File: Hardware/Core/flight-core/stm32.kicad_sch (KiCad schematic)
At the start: 33 parts, among them J1 Conn_01x04_Socket, SW1 SW_Push, SW2 SW_Push, U1 STM32G473CCTx, U13 MCP23S17_SS, U402 TCAN1042VDRQ1, U92 CC56-12SEKWA, U98 MAX7221xWG, Y1 48 MHZ

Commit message: updated all top sheets
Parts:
- removed TP_STM_IO2: TP, footprints:tp_1.6mm, symbol formula:TP
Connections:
- net CTRL_SANITY_CHECK is gone; now on net CORE_HEARTBEAT: U1.39 (PA15)
- net GPIO_SENSE3 is gone; now on net SHDN_SENSE_BMS_OK_ALL: U13.28 (GPA7)
- net CORE_HEARTBEAT: no longer U1.29 (PB15)
- net DEBUG1: now also U1.25 (PB11); no longer U1.28 (PB14)
- net DEBUG2: now also U13.22 (GPA1); no longer U13.27 (GPA6)
- net SHDN_SENSE_BMS_OK_ALL: no longer U13.26 (GPA5)
- net SHDN_SENSE_BMS_OK_E: now also U13.26 (GPA5); no longer U13.24 (GPA3)
- net SHDN_SENSE_BMS_OK_N: now also U13.25 (GPA4); no longer U13.23 (GPA2)
- net SHDN_SENSE_BMS_OK_S: now also U13.27 (GPA6); no longer U13.25 (GPA4)
- net SHDN_SENSE_E_ARM: no longer U1.42 (PB5)
- net SHDN_SENSE_NE_ARM: no longer U1.46 (PB9)
- net SHDN_SENSE_NUC: now also U13.24 (GPA3); no longer U13.22 (GPA1)
- net SHDN_SENSE_NW_ARM: no longer U1.16 (PB0)
- net SHDN_SENSE_SE_ARM: no longer U1.41 (PB4)
- net at U13.1 (GPB0): now also TP_STM_IO1.1 (TP)
- net SHDN_SENSE_SANITY renamed SHDN_SENSE_CTRL_CRIT
- new net CTRL_CRIT_CHECK: U1.28 (PB14)
- new net CTRL_NONCRIT_CHECK: U1.29 (PB15)
- new net SHDN_SENSE_CTRL_LOBATT: U13.23 (GPA2)
- new net SHDN_SENSE_N_ARM: U1.16 (PB0)
- new net SHDN_SENSE_SW_ARM: U1.42 (PB5)
- new net SHDN_SENSE_S_ARM: U1.41 (PB4)
- new net SHDN_SENSE_W_ARM: U1.46 (PB9)
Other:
- sheet LEDs and TPs renamed LEDs & TPs
- sheet LEDs & TPs ports: added +60V, SHDN_SENSE_CTRL_CRIT, SHDN_SENSE_CTRL_LOBATT; removed SHDN_SENSE_SANITY
- moved on the sheet: TP_STM_IO1

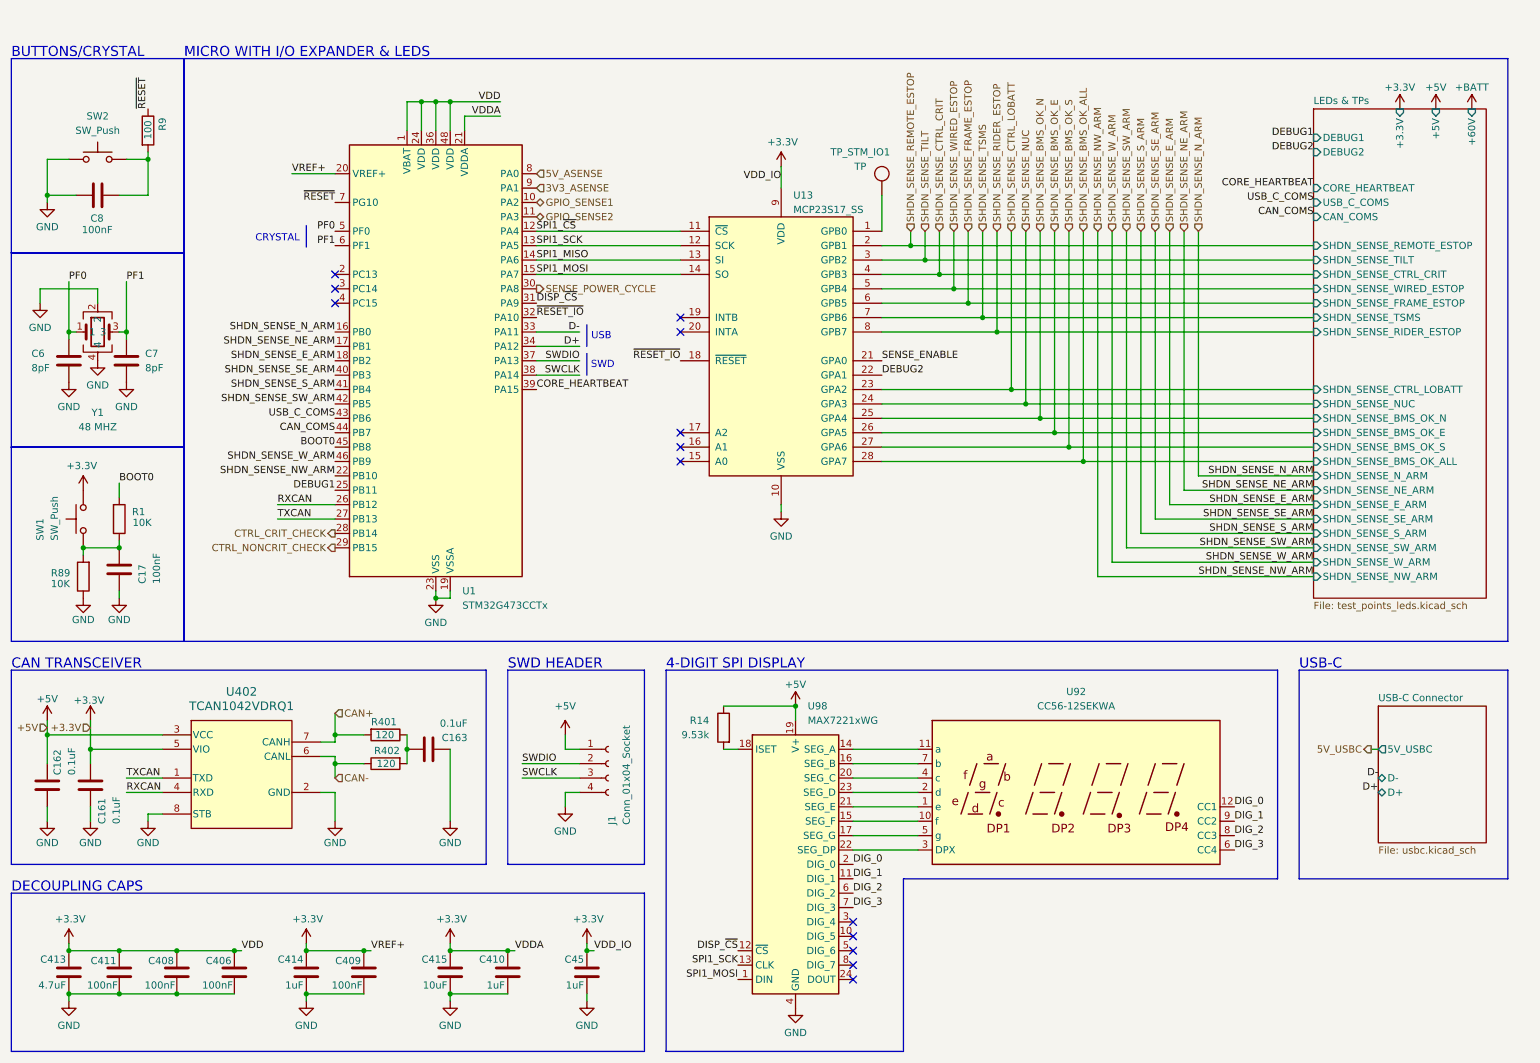
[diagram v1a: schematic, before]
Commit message: ERC fixes + reset cube signal
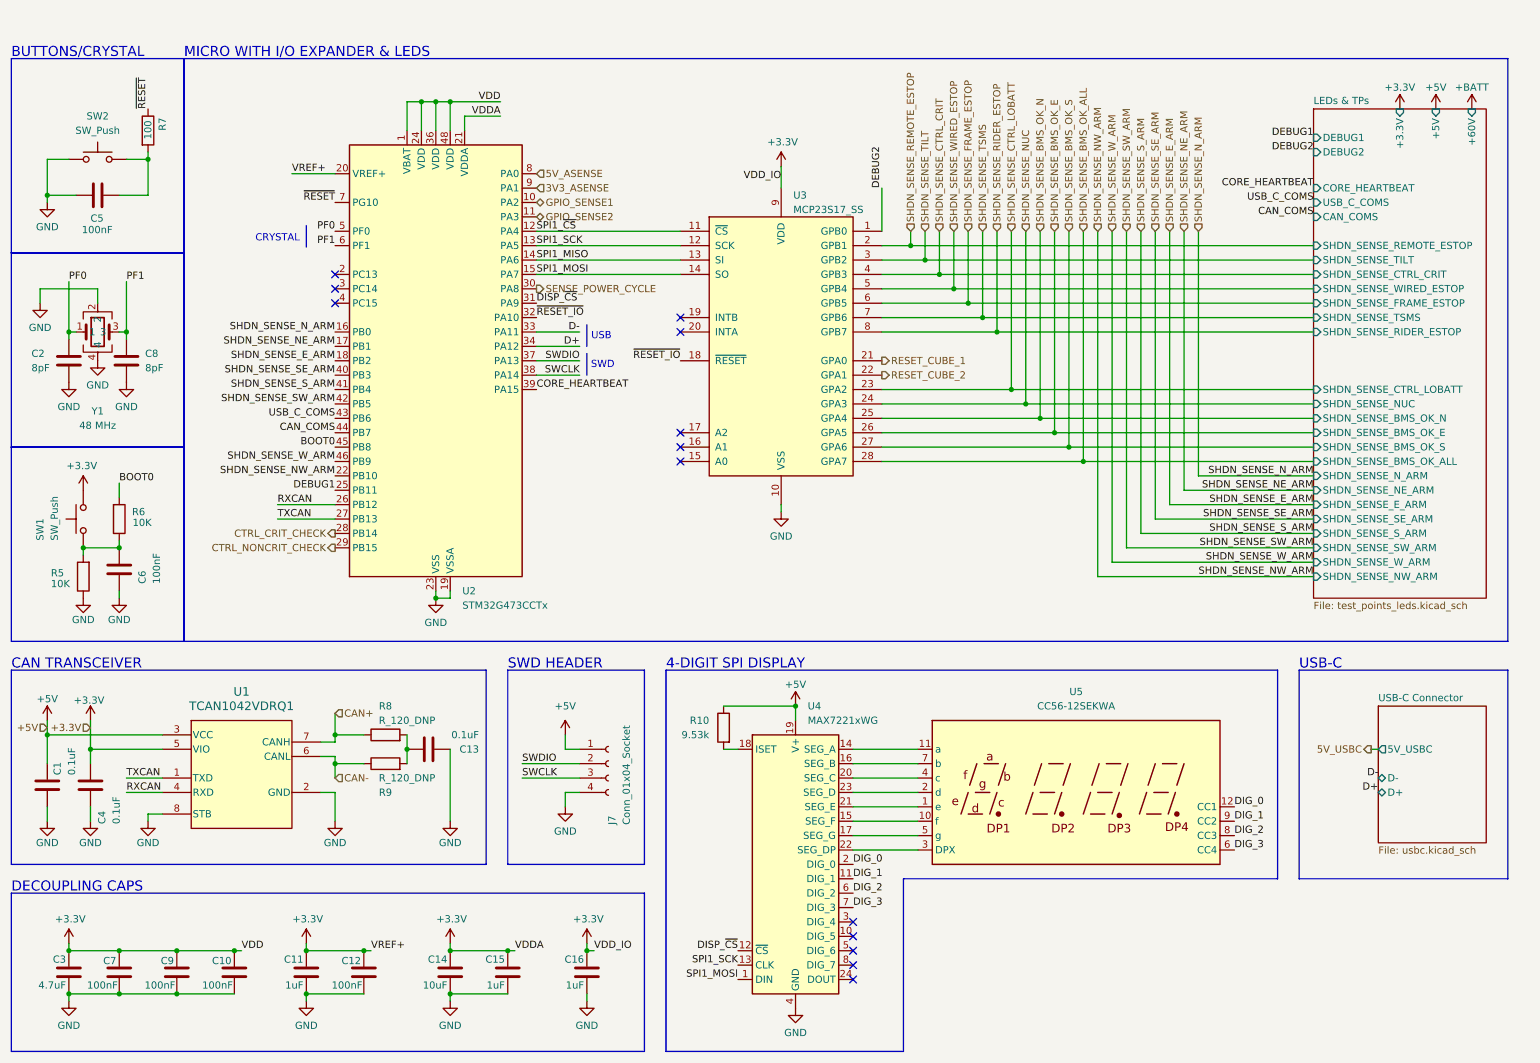
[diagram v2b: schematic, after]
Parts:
- removed R401, R402: 120, OEM:R_0603_1608Metric, symbol OEM:120R_DNP
- removed TP_STM_IO1: TP, footprints:tp_1.6mm, symbol formula:TP
- removed Y1: 48 MHZ, footprints:SMD_72002_TXC, symbol formula:Crystal_48MHz_8pF
- added R8, R9: R_120_DNP, footprints:R_0805_OEM, symbol formula:R_120_DNP
- added Y1: 48 MHz, footprints:Crystal_SMD_FA238, symbol OlinBAD:Crystal_48MHz_8pF_OBAD
- C10: renamed from C406; footprint Capacitor_SMD:C_0603_1608Metric -> footprints:C_0603_1608Metric
- C11: renamed from C414; footprint Capacitor_SMD:C_0603_1608Metric -> footprints:C_0603_1608Metric
- C12: renamed from C409; footprint Capacitor_SMD:C_0603_1608Metric -> footprints:C_0603_1608Metric
- C14: renamed from C415; footprint Capacitor_SMD:C_0805_2012Metric -> footprints:C_0603_1608Metric
- C15: renamed from C410; footprint Capacitor_SMD:C_0603_1608Metric -> footprints:C_0603_1608Metric
- C16: renamed from C45; footprint Capacitor_SMD:C_0603_1608Metric -> footprints:C_0603_1608Metric
- C3: renamed from C413; footprint Capacitor_SMD:C_0805_2012Metric -> footprints:C_0603_1608Metric
- C7: renamed from C411; footprint Capacitor_SMD:C_0603_1608Metric -> footprints:C_0603_1608Metric
- C9: renamed from C408; footprint Capacitor_SMD:C_0603_1608Metric -> footprints:C_0603_1608Metric
- R5: renamed from R89; footprint footprints:R_0805_OEM -> footprints:R_0603_1608Metric
- R6: renamed from R1; footprint footprints:R_0805_OEM -> footprints:R_0603_1608Metric
- R7: renamed from R9; footprint footprints:R_0805_OEM -> footprints:R_0603_1608Metric
- SW1, SW2: footprint (none) -> Button_Switch_SMD:SW_Push_1P1T_NO_CK_KMR2
- U1: renamed from U402; footprint BAD_LIB:D0008A_M -> obad_footprints:D0008A_M
- renumbered C162 to C1, C163 to C13, C6 to C2, C161 to C4, C8 to C5, C17 to C6, C7 to C8, J1 to J7, R14 to R10, U1 to U2, U13 to U3, U98 to U4, U92 to U5
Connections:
- net CAN+: now also R8.1
- net CAN-: now also R9.1
- net DEBUG2: now also U3.1 (GPB0); no longer U3.22 (GPA1)
- net GND: now also Y1.2, Y1.4
- net PF0: now also Y1.1
- net PF1: now also Y1.3
- net at C13.1: now also R8.2, R9.2
- net SENSE_ENABLE renamed RESET_CUBE_1
- new net RESET_CUBE_2: U3.22 (GPA1)

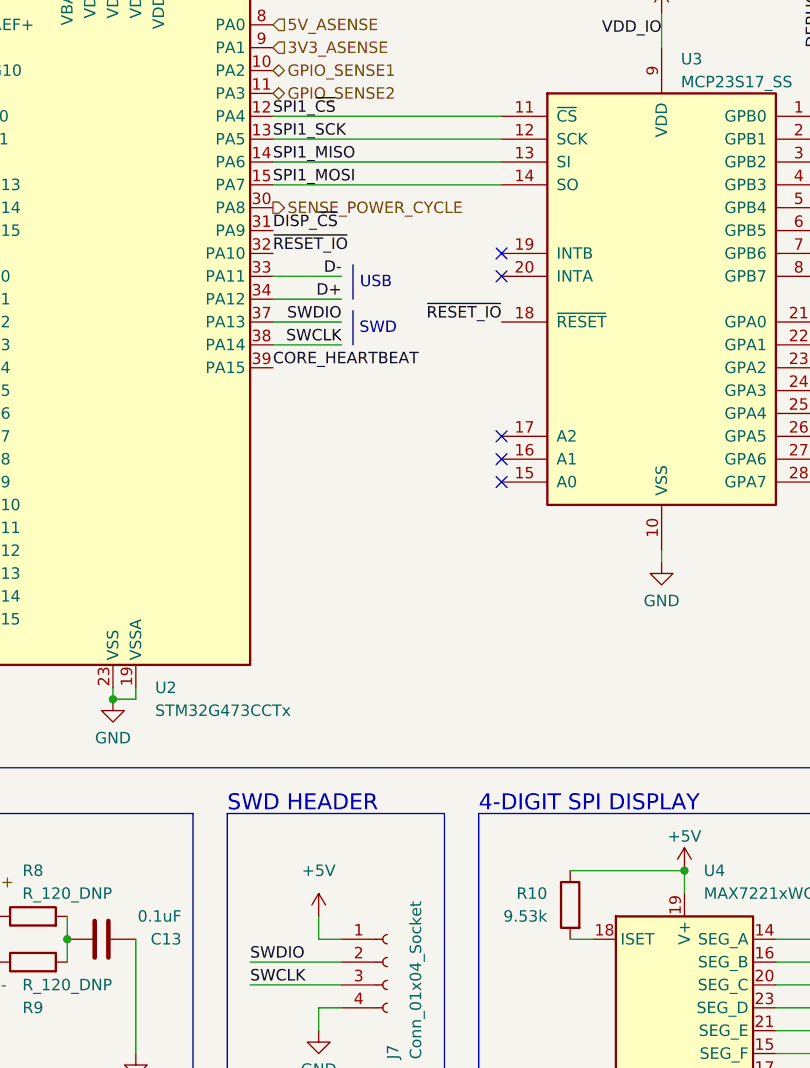
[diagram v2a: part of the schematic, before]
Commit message: added sense pwr cycle pull down, low side cube mosfets, fixed mosi/miso swap on i/o expander, Rs -> generic, reannotated
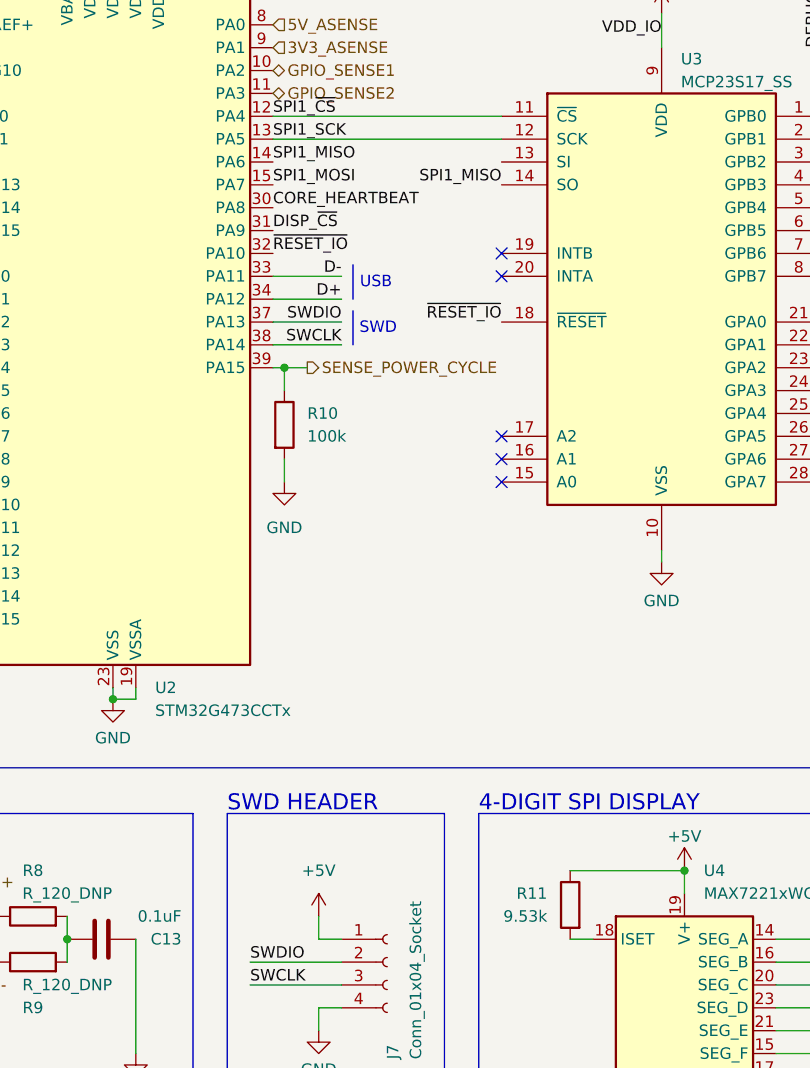
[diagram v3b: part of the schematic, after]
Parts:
- added R10: 100k, footprints:R_0603_1608Metric, symbol Device:R
- renumbered R10 to R11
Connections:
- net CORE_HEARTBEAT: now also U2.30 (PA8); no longer U2.39 (PA15)
- net GND: now also R10.2
- net SENSE_POWER_CYCLE: now also U2.39 (PA15), R10.1; no longer U2.30 (PA8)
- net SPI1_MISO: now also U3.14 (SO); no longer U3.13 (SI)
- net SPI1_MOSI: no longer U3.14 (SO)
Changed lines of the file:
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@@
 	)
 	(junction
+		(at 110.49 77.47)
+		(diameter 0)
+		(color 0 0 0 0)
+	)
+	(junction
 		(at 73.66 143.51)
 		(diameter 0)
@@
 	(wire
 		(pts
-			(xy 109.22 57.15) (xy 134.62 57.15)
-		)
-		(stroke
-			(width 0)
-			(type default)
-		)
-	)
-	(wire
-		(pts
 			(xy 73.66 143.51) (xy 73.66 146.05)
 		)
@@
 		)
 	)
-	(wire
-		(pts
-			(xy 109.22 54.61) (xy 134.62 54.61)
-		)
-		(stroke
-			(width 0)
-			(type default)
-		)
-	)
 	(bus
 		(pts
@@
 	(wire
 		(pts
+			(xy 110.49 77.47) (xy 109.22 77.47)
+		)
+		(stroke
+			(width 0)
+			(type default)
+		)
+	)
+	(wire
+		(pts
 			(xy 165.1 156.21) (xy 176.53 156.21)
 		)
@@
 	(wire
 		(pts
+			(xy 113.03 77.47) (xy 110.49 77.47)
+		)
+		(stroke
+			(width 0)
+			(type default)
+		)
+	)
+	(wire
+		(pts
 			(xy 152.4 38.1) (xy 152.4 41.91)
 		)
@@
 	(wire
 		(pts
+			(xy 110.49 87.63) (xy 110.49 90.17)
+		)
+		(stroke
+			(width 0)
+			(type default)
+		)
+	)
+	(wire
+		(pts
 			(xy 35.56 104.14) (xy 35.56 105.41)
 		)
@@
 	(wire
 		(pts
+			(xy 110.49 77.47) (xy 110.49 80.01)
+		)
+		(stroke
+			(width 0)
+			(type default)
+		)
+	)
+	(wire
+		(pts
 			(xy 118.11 176.53) (xy 119.38 176.53)
 		)
@@
 		)
 	)
+	(label "SPI1_MISO"
+		(at 134.62 57.15 180)
+		(effects
+			(font
+				(size 1.27 1.27)
+			)
+			(justify right bottom)
+		)
+	)
 	(label "CAN_COMS"
 		(at 246.38 46.99 180)
@@
 	)
 	(label "CORE_HEARTBEAT"
-		(at 109.22 77.47 0)
+		(at 109.22 59.69 0)
 		(effects
 			(font
@@
 	(hierarchical_label "SENSE_POWER_CYCLE"
 		(shape output)
-		(at 109.22 59.69 0)
+		(at 113.03 77.47 0)
 		(effects
 			(font
@@
 	)
 	(symbol
+		(lib_id "power:GND")
+		(at 110.49 90.17 0)
+		(unit 1)
+		(exclude_from_sim no)
+		(in_bom yes)
+		(on_board yes)
+		(dnp no)
+		(fields_autoplaced yes)
+		(property "Reference" "#PWR0449"
+			(at 110.49 96.52 0)
+			(effects
+				(font
+					(size 1.27 1.27)
+				)
+				(hide yes)
+			)
+		)
+		(property "Value" "GND"
+			(at 110.49 95.25 0)
+			(effects
+				(font
+					(size 1.27 1.27)
+				)
+			)
+		)
+		(property "Footprint" ""
+			(at 110.49 90.17 0)
+			(effects
+				(font
+					(size 1.27 1.27)
+				)
+				(hide yes)
+			)
+		)
+		(property "Datasheet" ""
+			(at 110.49 90.17 0)
+			(effects
+				(font
+					(size 1.27 1.27)
+				)
+				(hide yes)
+			)
+		)
+		(property "Description" "Power symbol creates a global label with name \"GND\" , ground"
+			(at 110.49 90.17 0)
+			(effects
+				(font
+					(size 1.27 1.27)
+				)
+				(hide yes)
+			)
+		)
+		(pin "1"
+		)
+		(instances
+			(project ""
+				(path "/93f46f4b-cdf5-47ec-af03-96378e73b2e1/91e18f07-bd3f-4576-bbe1-a0227cf7132e"
+					(reference "#PWR0449")
+					(unit 1)
+				)
+			)
+		)
+	)
+	(symbol
 		(lib_id "formula:C_10uF")
 		(at 68.58 181.61 0)
@@
 	)
 	(symbol
+		(lib_id "Device:R")
+		(at 110.49 83.82 0)
+		(unit 1)
+		(exclude_from_sim no)
+		(in_bom yes)
+		(on_board yes)
+		(dnp no)
+		(fields_autoplaced yes)
+		(property "Reference" "R10"
+			(at 113.03 82.5499 0)
+			(effects
+				(font
+					(size 1.27 1.27)
+				)
+				(justify left)
+			)
+		)
+		(property "Value" "100k"
+			(at 113.03 85.0899 0)
+			(effects
+				(font
+					(size 1.27 1.27)
+				)
+				(justify left)
+			)
+		)
+		(property "Footprint" "footprints:R_0603_1608Metric"
+			(at 108.712 83.82 90)
+			(effects
+				(font
+					(size 1.27 1.27)
+				)
+				(hide yes)
+			)
+		)
+		(property "Datasheet" "~"
+			(at 110.49 83.82 0)
+			(effects
+				(font
+					(size 1.27 1.27)
+				)
+				(hide yes)
+			)
+		)
+		(property "Description" "Resistor"
+			(at 110.49 83.82 0)
+			(effects
+				(font
+					(size 1.27 1.27)
+				)
+				(hide yes)
+			)
+		)
+		(pin "1"
+		)
+		(pin "2"
+		)
+		(instances
+			(project ""
+				(path "/93f46f4b-cdf5-47ec-af03-96378e73b2e1/91e18f07-bd3f-4576-bbe1-a0227cf7132e"
+					(reference "R10")
+					(unit 1)
+				)
+			)
+		)
+	)
+	(symbol
 		(lib_id "power:GND")
 		(at 26.67 76.2 0)
@@
 		(on_board yes)
 		(dnp no)
-		(property "Reference" "R10"
+		(property "Reference" "R11"
 			(at 139.7 135.89 0)
 			(effects
@@
 			(project ""
 				(path "/93f46f4b-cdf5-47ec-af03-96378e73b2e1/91e18f07-bd3f-4576-bbe1-a0227cf7132e"
-					(reference "R10")
+					(reference "R11")
 					(unit 1)
 				)
